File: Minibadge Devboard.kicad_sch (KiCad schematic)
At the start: 44 parts, among them J1 External power, J2 External switch, SW1 Power, SW3 SPEED, SW4 NTC

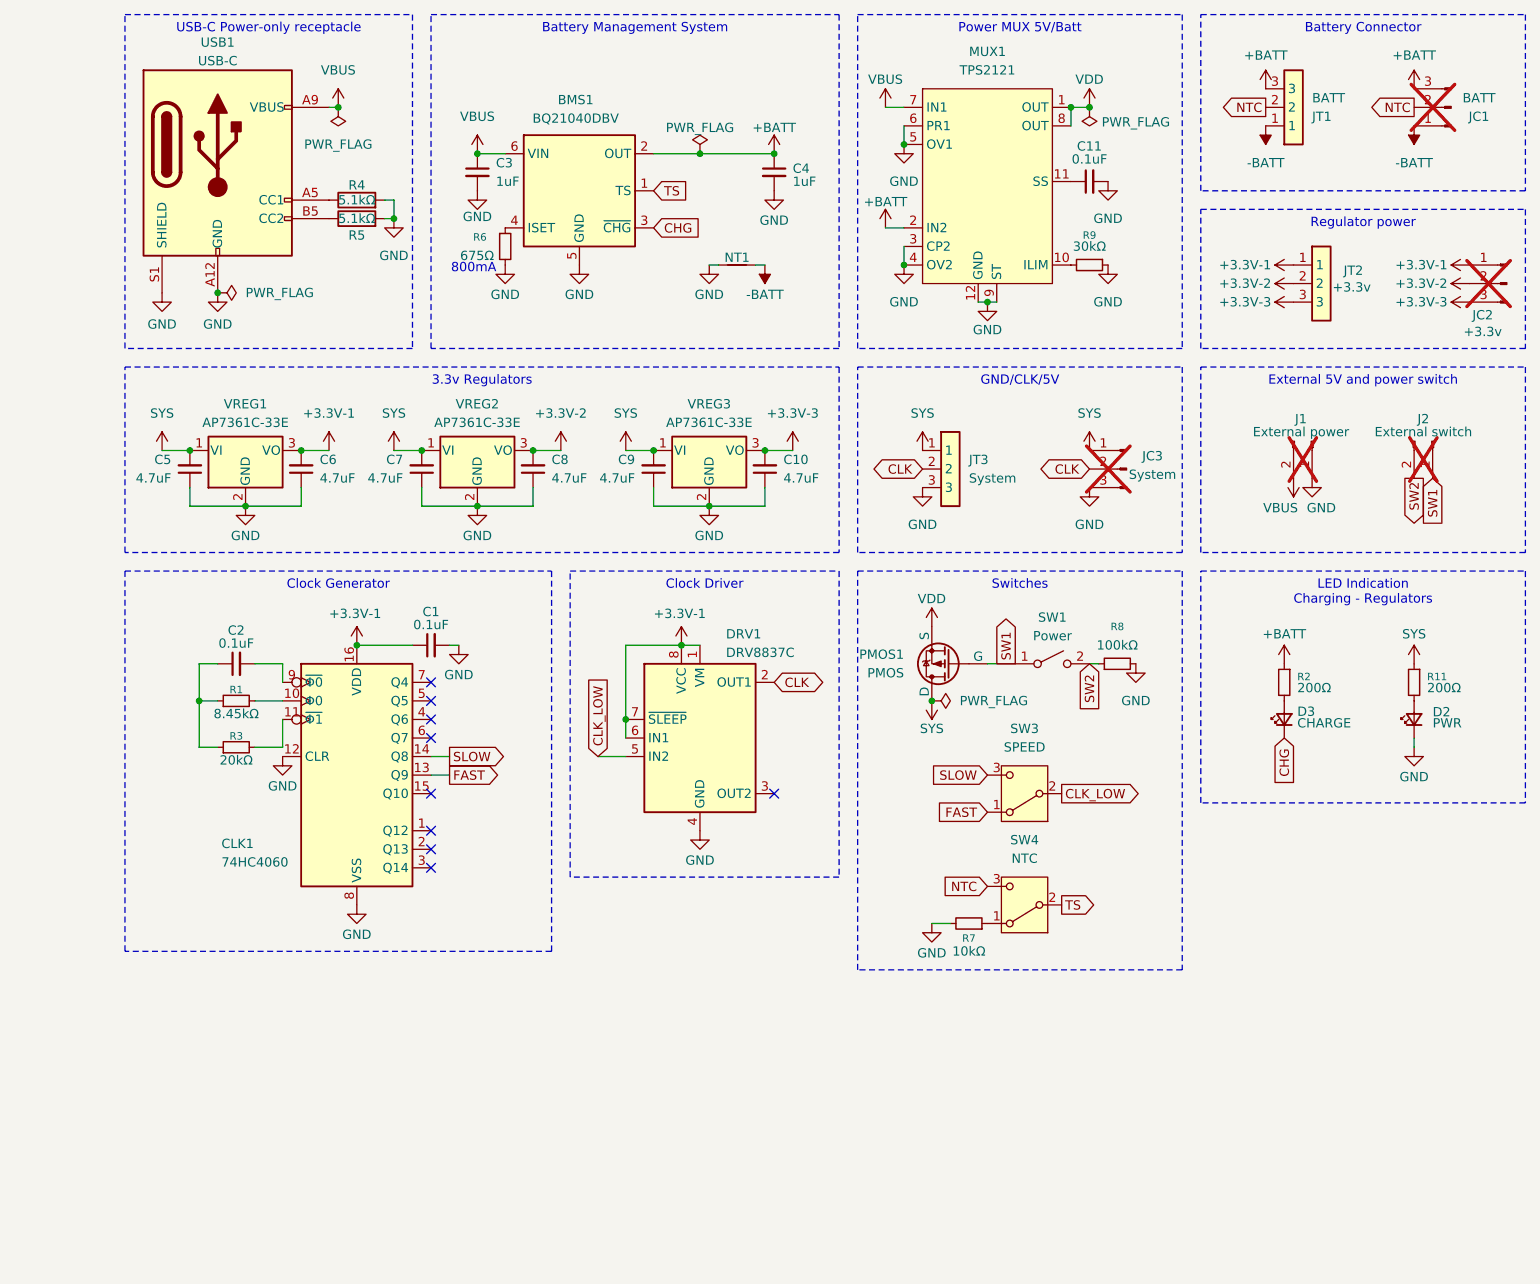
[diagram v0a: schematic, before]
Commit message: Swap LDO to DC-DC
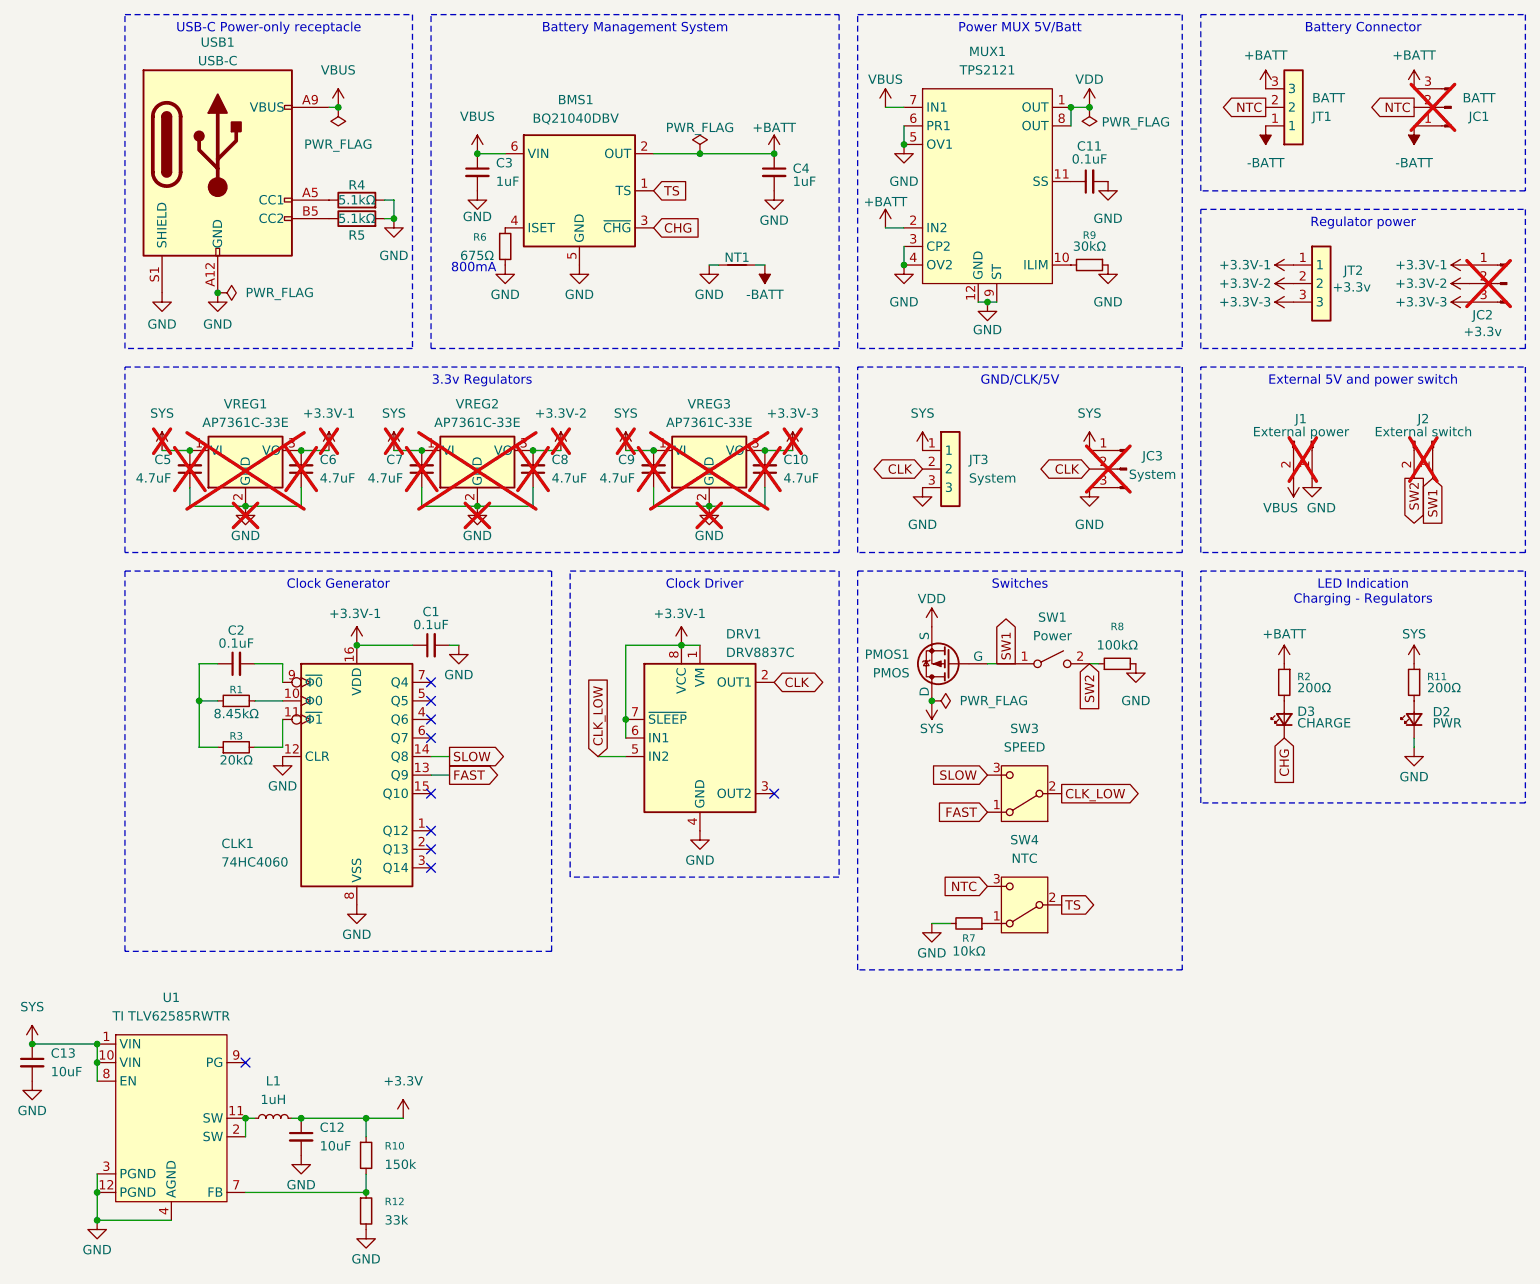
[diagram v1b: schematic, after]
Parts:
- added C12, C13: 10uF, Capacitor_SMD:C_0805_2012Metric, symbol Device:C_Small
- added L1: 1uH, Inductor_SMD:L_6.3x6.3_H3, symbol Device:L_Small
- added R10: 150k, Resistor_SMD:R_0603_1608Metric, symbol Device:R_Small
- added R12: 33k, Resistor_SMD:R_0603_1608Metric, symbol Device:R_Small
- added U1: TI TLV62585RWTR, TI TLV62585RWTR:TLV62585RWTR, symbol TLV62585RWTR:TLV62585
- C10, C5, C6, C7, C8, C9, VREG1, VREG2, VREG3: now not fitted; now left out of the parts list
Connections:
- net GND: now also C12.2, C13.2, R12.2, U1.12 (PGND), U1.3 (PGND), U1.4 (AGND)
- net SYS: now also C13.1, U1.1 (VIN), U1.10 (VIN), U1.8 (EN)
- new net: L1.1, U1.11 (SW), U1.2 (SW)
- new net: R10.2, R12.1, U1.7 (FB)
- new net +3.3V: C12.1, L1.2, R10.1
- no-connect marks 9 -> 10

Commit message: Implement/route DC-DC buck
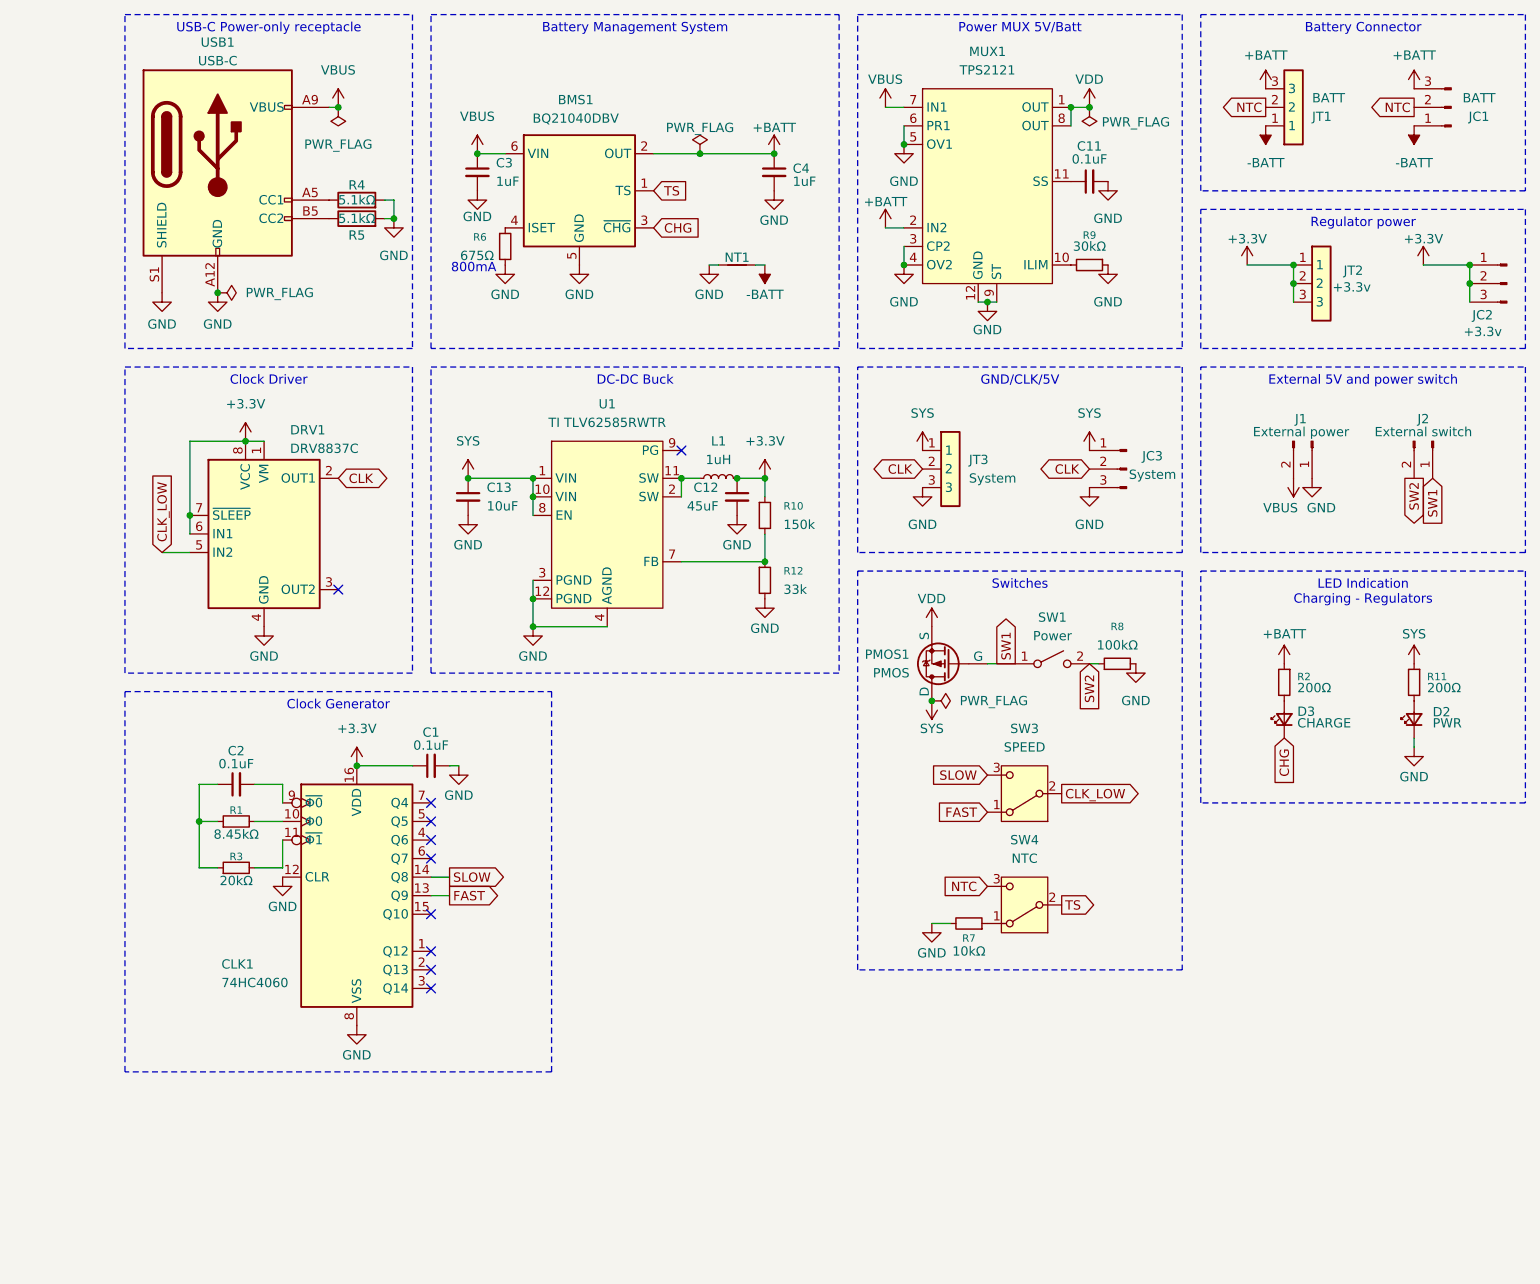
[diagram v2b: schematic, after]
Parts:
- removed C10, C5, C6, C7, C8, C9: 4.7uF, Capacitor_SMD:C_0805_2012Metric, symbol Device:C_Small
- removed VREG1, VREG2, VREG3: AP7361C-33E, Package_TO_SOT_SMD:SOT-223-3_TabPin2, symbol Regulator_Linear:AP7361C-33E
- C12: value 10uF -> 45uF; footprint Capacitor_SMD:C_0805_2012Metric -> Capacitor_SMD:C_1206_3216Metric
- C13: footprint Capacitor_SMD:C_0805_2012Metric -> Capacitor_SMD:C_1206_3216Metric
- J1, J2, JC1, JC2, JC3: now fitted
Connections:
- net +3.3V-1 is gone; now on net +3.3V: C1.1, CLK1.16 (VDD), DRV1.1 (VM), DRV1.6 (IN1), DRV1.7 (~{SLEEP}), DRV1.8 (VCC), JC2.1 (Pin_1), JT2.1
- net +3.3V-2 is gone; now on net +3.3V: JC2.2 (Pin_2), JT2.2
- net +3.3V-3 is gone; now on net +3.3V: JC2.3 (Pin_3), JT2.3
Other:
- moved on the sheet: C1, C12, C13, C2, CLK1, DRV1, R1, R10, R12, R3, U1

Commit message: LCSC part numbers
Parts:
- C12: value 45uF -> 47uF; LCSC Part # (none) -> C96123
- C13: value 10uF -> 47uF; LCSC Part # (none) -> C96123
- R10: LCSC Part # (none) -> C22807
- R12: LCSC Part # (none) -> C4216
- renumbered U1 to BUCK1
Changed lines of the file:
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@@
 			)
 		)
-		(property "LCSC Part #" ""
+		(property "LCSC Part #" "C22807"
 			(at 146.05 91.44 0)
 			(effects
@@
 		(dnp no)
 		(fields_autoplaced yes)
-		(property "Reference" "U1"
+		(property "Reference" "BUCK1"
 			(at 124.46 76.2 0)
 			(effects
@@
 			(project ""
 				(path "/5e8d5e65-6836-49cf-87c9-8c3c5b8fcf7b"
-					(reference "U1")
+					(reference "BUCK1")
 					(unit 1)
 				)
@@
 			)
 		)
-		(property "LCSC Part #" ""
+		(property "LCSC Part #" "C4216"
 			(at 146.05 100.33 0)
 			(effects
@@
 			)
 		)
-		(property "Value" "45uF"
+		(property "Value" "47uF"
 			(at 139.7 90.1762 0)
 			(effects
@@
 			)
 		)
-		(property "LCSC Part #" ""
+		(property "LCSC Part #" "C96123"
 			(at 142.24 88.9 0)
 			(effects
@@
 			)
 		)
-		(property "Value" "10uF"
+		(property "Value" "47uF"
 			(at 107.95 90.1762 0)
 			(effects
@@
 			)
 		)
-		(property "LCSC Part #" ""
+		(property "LCSC Part #" "C96123"
 			(at 105.41 88.9 0)
 			(effects

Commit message: Update inductor
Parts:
- L1: footprint Inductor_SMD:L_6.3x6.3_H3 -> Inductor_SMD:L_KOHERelec_MDA5030; LCSC Part # (none) -> C2847474
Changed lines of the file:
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@@
 			)
 		)
-		(property "Footprint" "Inductor_SMD:L_6.3x6.3_H3"
+		(property "Footprint" "Inductor_SMD:L_KOHERelec_MDA5030"
 			(at 139.7 86.36 0)
 			(effects
@@
 			)
 		)
-		(property "LCSC Part #" ""
+		(property "LCSC Part #" "C2847474"
 			(at 139.7 86.36 0)
 			(effects

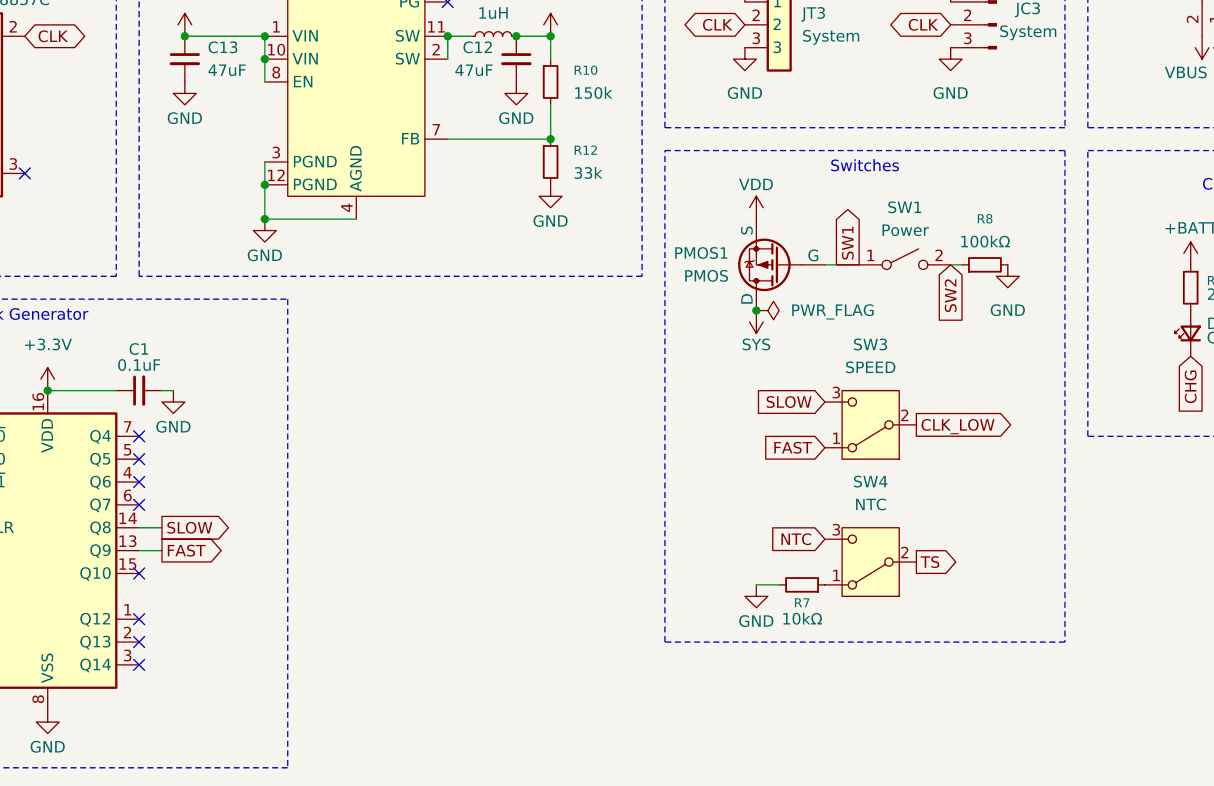
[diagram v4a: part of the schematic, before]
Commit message: Updates
* Fix fast/slow in schematic
* Fix footprint/schematic issue with WAGO connector
* Fix update WAGO connector footprint
* Fix SW1 GND pads
* Fix via placement on WAGO pads
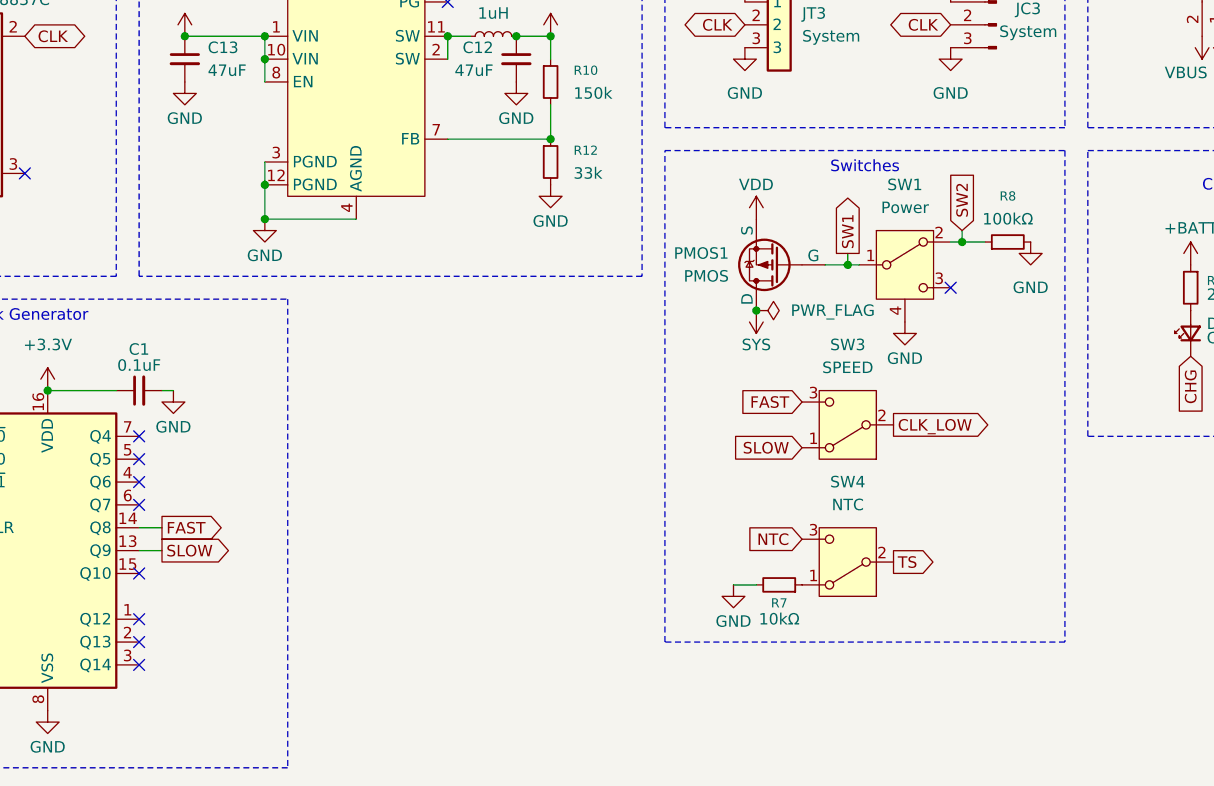
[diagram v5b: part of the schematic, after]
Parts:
- JT1, JT2, JT3: footprint WAGO 2059-303:2059-303 -> WAGO 2059-303:WAGO 2059-303
- SW1: symbol Switch:SW_SPST -> Switch:SW_SPDT
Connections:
- net FAST: now also CLK1.14 (Q8), SW3.3 (C); no longer CLK1.13 (Q9), SW3.1 (A)
- net GND: now also SW1.4
- net SLOW: now also CLK1.13 (Q9), SW3.1 (A); no longer CLK1.14 (Q8), SW3.3 (C)
- no-connect marks 10 -> 11
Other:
- moved on the sheet: R7, R8, SW3, SW4
